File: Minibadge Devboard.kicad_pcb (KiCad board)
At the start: 2 copper layers, 30.5 x 45.8 mm, 51 parts, among them J1 External power, J2 External switch, SW1 Power, SW3 SPEED, SW4 NTC

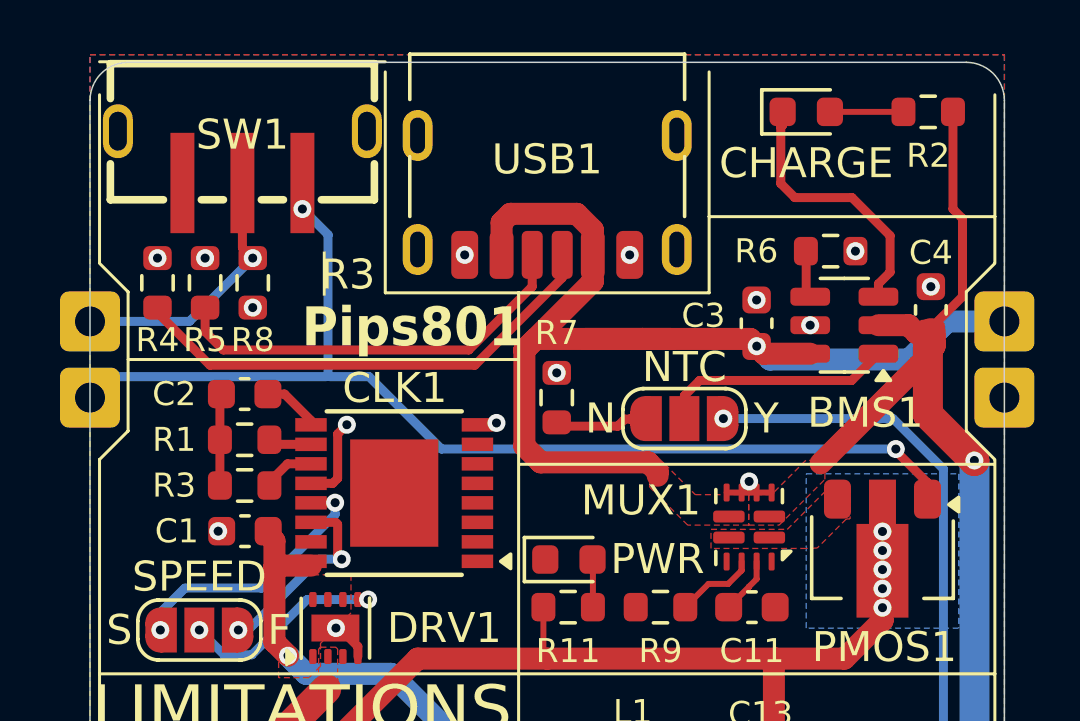
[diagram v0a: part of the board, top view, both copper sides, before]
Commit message: Fix SW1
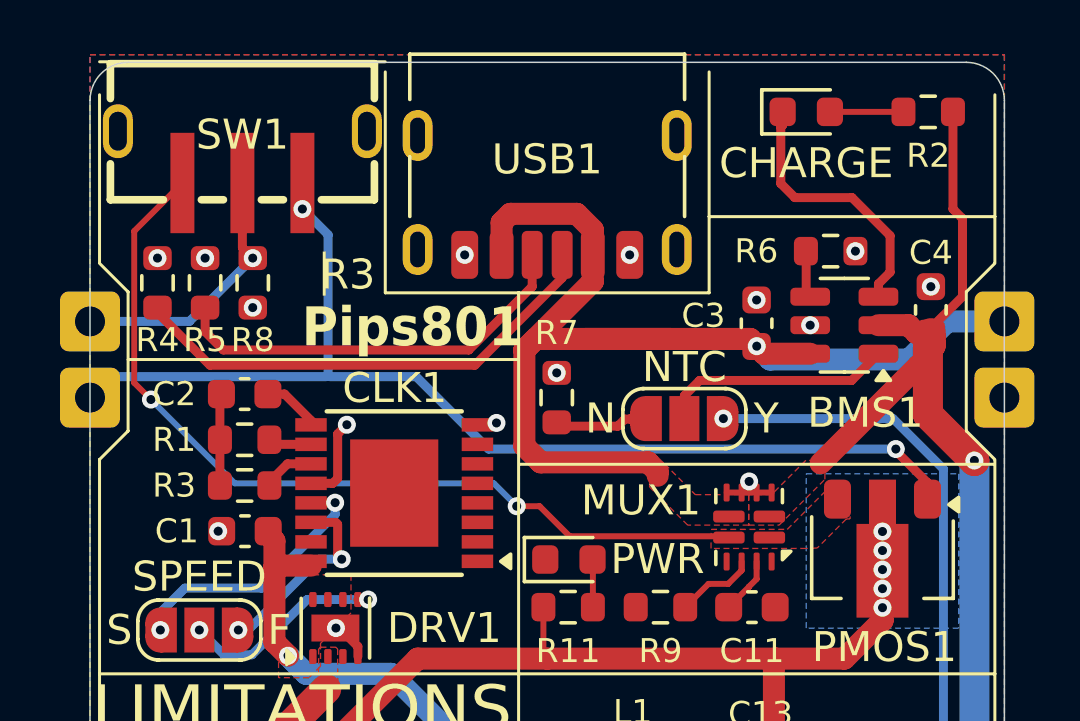
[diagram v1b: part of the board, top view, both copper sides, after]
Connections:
- SW1 pad 3: unconnected-(SW1-C-Pad3) -> VDD
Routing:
- net VDD: track 0.00 -> 29.3 mm, vias 0 -> 2
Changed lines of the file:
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@@
 	(net 39 "unconnected-(BUCK1-PG-Pad9)")
 	(net 40 "Net-(BUCK1-FB)")
-	(net 41 "unconnected-(SW1-C-Pad3)")
 	(footprint "Capacitor_SMD:C_0603_1608Metric"
 		(layer "F.Cu")
@@
 			(size 0.8 3.345)
 			(layers "F.Cu" "F.Mask" "F.Paste")
-			(net 41 "unconnected-(SW1-C-Pad3)")
+			(net 26 "VDD")
 			(pinfunction "C")
-			(pintype "passive+no_connect")
+			(pintype "passive")
 		)
 		(pad "4" thru_hole oval
@@
 	)
 	(segment
+		(start 90.373416 46.177416)
+		(end 90.373416 41.125084)
+		(width 0.2)
+		(layer "F.Cu")
+		(net 26)
+	)
+	(segment
+		(start 103.124 50.292)
+		(end 103.886 50.292)
+		(width 0.2)
+		(layer "F.Cu")
+		(net 26)
+	)
+	(segment
+		(start 110.153911 51.294)
+		(end 110.196 51.336089)
+		(width 0.2)
+		(layer "F.Cu")
+		(net 26)
+	)
+	(segment
+		(start 90.932 46.736)
+		(end 90.373416 46.177416)
+		(width 0.2)
+		(layer "F.Cu")
+		(net 26)
+	)
+	(segment
+		(start 104.888 51.294)
+		(end 110.153911 51.294)
+		(width 0.2)
+		(layer "F.Cu")
+		(net 26)
+	)
+	(segment
+		(start 103.886 50.292)
+		(end 104.888 51.294)
+		(width 0.2)
+		(layer "F.Cu")
+		(net 26)
+	)
+	(segment
+		(start 90.373416 41.125084)
+		(end 91.98 39.5185)
+		(width 0.2)
+		(layer "F.Cu")
+		(net 26)
+	)
+	(via
+		(at 90.932 46.736)
+		(size 0.6)
+		(drill 0.3)
+		(layers "F.Cu" "B.Cu")
+		(net 26)
+	)
+	(via
+		(at 103.124 50.292)
+		(size 0.6)
+		(drill 0.3)
+		(layers "F.Cu" "B.Cu")
+		(net 26)
+	)
+	(segment
+		(start 102.362 49.53)
+		(end 93.726 49.53)
+		(width 0.2)
+		(layer "B.Cu")
+		(net 26)
+	)
+	(segment
+		(start 93.726 49.53)
+		(end 90.932 46.736)
+		(width 0.2)
+		(layer "B.Cu")
+		(net 26)
+	)
+	(segment
+		(start 103.124 50.292)
+		(end 102.362 49.53)
+		(width 0.2)
+		(layer "B.Cu")
+		(net 26)
+	)
+	(segment
 		(start 93.98 40.441)
 		(end 93.98 41.677636)
@@
 	)
 	(segment
-		(start 100.616 48.387)
-		(end 115.7605 48.387)
-		(width 0.3)
-		(layer "B.Cu")
-		(net 28)
-	)
-	(segment
 		(start 96.8375 41.2435)
 		(end 96.8375 45.9105)
@@
 	(segment
 		(start 96.901 45.974)
-		(end 98.203 45.974)
+		(end 99.7745 45.974)
 		(width 0.3)
 		(layer "B.Cu")
@@
 	)
 	(segment
-		(start 96.8375 45.9105)
-		(end 96.901 45.974)
+		(start 99.7745 45.974)
+		(end 102.1875 48.387)
 		(width 0.3)
 		(layer "B.Cu")
@@
 	)
 	(segment
-		(start 95.98 40.386)
-		(end 96.8375 41.2435)
+		(start 102.1875 48.387)
+		(end 115.7605 48.387)
 		(width 0.3)
 		(layer "B.Cu")
@@
 	)
 	(segment
-		(start 98.203 45.974)
-		(end 100.616 48.387)
+		(start 96.8375 45.9105)
+		(end 96.901 45.974)
+		(width 0.3)
+		(layer "B.Cu")
+		(net 28)
+	)
+	(segment
+		(start 95.98 40.386)
+		(end 96.8375 41.2435)
 		(width 0.3)
 		(layer "B.Cu")

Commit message: update PDF
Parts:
- added R13: 1MΩ, Resistor_SMD:R_0603_1608Metric, F.Cu at (95.5, 42.9)
- moved R8 3.39 mm to (90.9, 42.9)
- moved R4 1.31 mm to (92.5, 42.9)
- moved R5 1.25 mm to (94.0, 42.9)
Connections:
- PMOS1 pad 1: SW1 -> SW2
- R8 pad 1: SW2 -> GND
- R8 pad 2: GND -> SW1
- SW1 pad 1: SW1 -> unconnected-(SW1-A-Pad1)
- SW1 pad 3: VDD -> SW1
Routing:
- net SW2: track 7.37 -> 35.3 mm, vias 1 -> 3
- net SW1: track 36.1 -> 8.43 mm
- net VDD: track 29.3 -> 17.9 mm
- net Net-(USB1-CC2): track 13.9 -> 12.6 mm
- net Net-(USB1-CC1): track 16.4 -> 15.3 mm
- net unconnected-(SW1-A-Pad1): vias 0 -> 1
- net GND: vias 17 -> 16
